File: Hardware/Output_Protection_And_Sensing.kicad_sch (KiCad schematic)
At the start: 8 parts

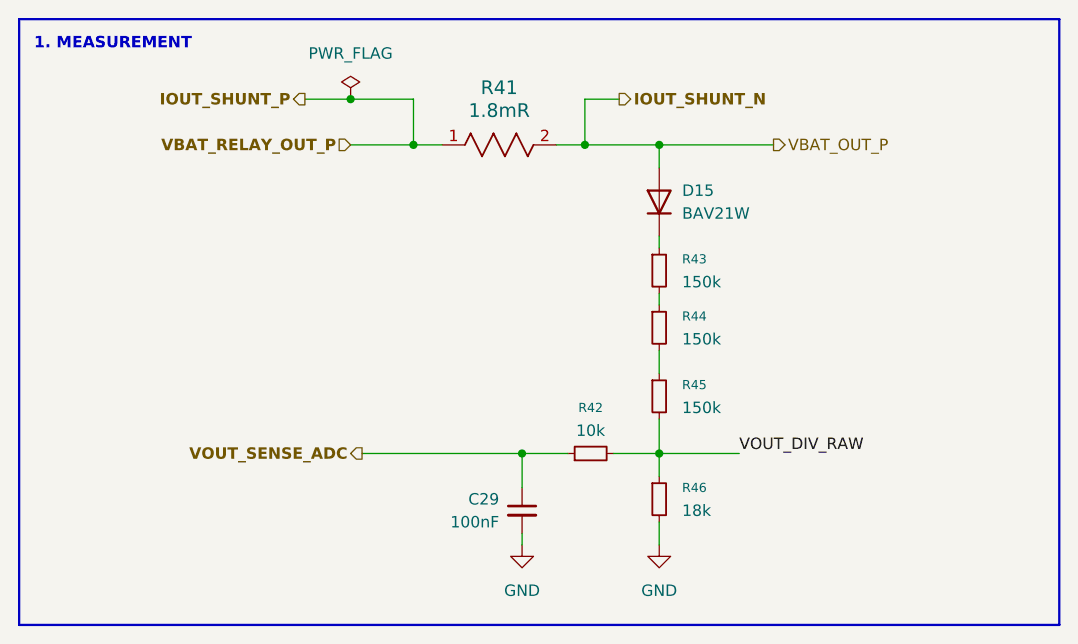
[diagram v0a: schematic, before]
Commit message: feat: update buy link, footprint
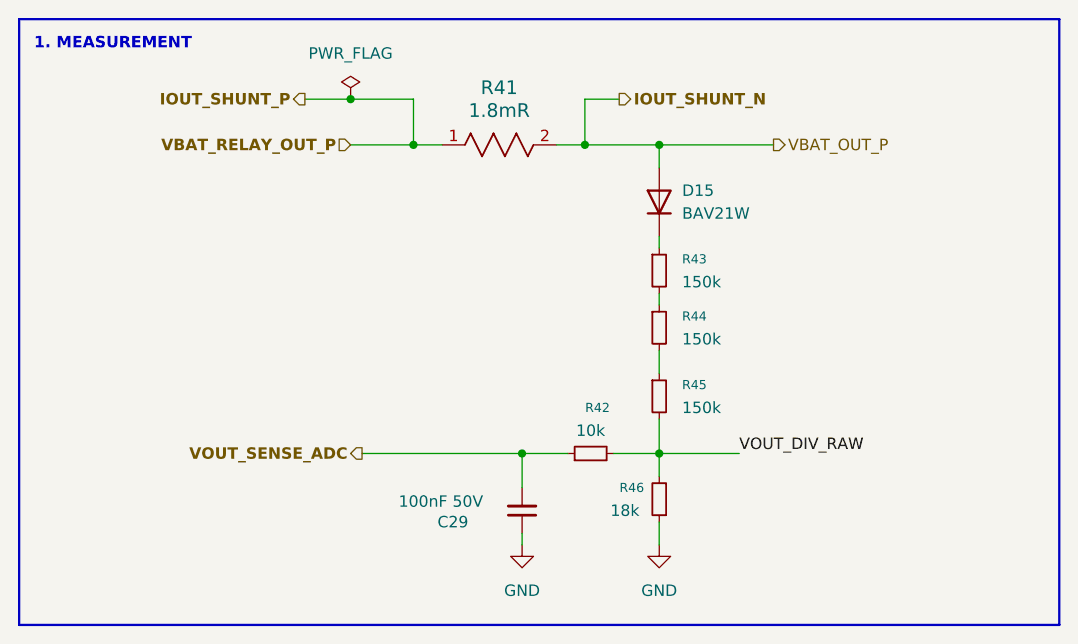
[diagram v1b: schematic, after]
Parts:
- C29: value 100nF -> 100nF 50V; footprint (none) -> Capacitor_SMD:C_0805_2012Metric; Link to Buy (none) -> https://linhkien.cxtvn.com/1976-tu-khong-phan-cuc-0805.html
- D15: footprint Diode_THT:D_DO-35_SOD27_P7.62mm_Horizontal -> Diode_SMD:D_SOD-123; Link to Buy (none) -> https://linhkienthuduc.com/san-pham/bav21w-250v-400ma-sod-1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
- R41: Link to Buy (none) -> https://www.lcsc.com/product-detail/C6490493.html?s_z=n_q_p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
- R42: footprint (none) -> Resistor_SMD:R_0805_2012Metric; Link to Buy (none) -> https://linhkien.cxtvn.com/8792-dien-tro-10k-0805-01-10c.ht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
- R43, R44, R45: footprint (none) -> Resistor_SMD:R_0805_2012Metric; Link to Buy (none) -> https://linhkien.cxtvn.com/6685-dien-tro-0805-1-thong-so-tu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
- R46: footprint (none) -> Resistor_SMD:R_0805_2012Metric; Link to Buy (none) -> https://linhkien.cxtvn.com/4177-dien-tro-0805-1-thong-so-tu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
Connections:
- net GND: now also C29.1, R46.1; no longer C29.2, R46.2
- net VOUT_DIV_RAW: now also R46.2; no longer R46.1
- net VOUT_SENSE_ADC: now also C29.2; no longer C29.1

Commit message: feat: update schematic with new components for communication interfaces and export BOM list
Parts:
- C29: value 100nF 50V -> 100nF
- R41: footprint RES_1L00x_BRN -> CSS2H_2512R_1L00F:RES_1L00x_BRN
- R42: value 10k -> 10kR; Link to Buy https://linhkien.cxtvn.com/8792-dien-tro-10k-0805-01-10c.ht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 -> https://linhkien.cxtvn.com/9909-dien-tro-0805-05-18w-10-chi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
- R43, R44, R45: value 150k -> 150kR
- R46: value 18k -> 18kR
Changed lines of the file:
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@@
 			)
 		)
-		(property "Footprint" "RES_1L00x_BRN"
+		(property "Footprint" "CSS2H_2512R_1L00F:RES_1L00x_BRN"
 			(at 135.89 74.93 0)
 			(hide yes)
@@
 			)
 		)
-		(property "Datasheet" "https://mm.digikey.com/Volume0/opasdata/d220001/medias/docus/5561/BAV19W%20thru%20BAV21W.pdf"
+		(property "Datasheet" "https://mm.digikey.com/Volume0/opasdata/d220001/medias/docus/5335/SOD123AV21WST3.pdf"
 			(at 160.02 81.28 0)
 			(hide yes)
@@
 			)
 		)
-		(property "Value" "10k"
+		(property "Value" "10kR"
 			(at 152.4 106.68 90)
 			(show_name no)
@@
 			)
 		)
-		(property "Link to Buy" "https://linhkien.cxtvn.com/8792-dien-tro-10k-0805-01-10c.html"
+		(property "Link to Buy" "https://linhkien.cxtvn.com/9909-dien-tro-0805-05-18w-10-chiec-cac-gia-tri.html"
 			(at 234.95 -85.09 0)
 			(hide yes)
@@
 			)
 		)
-		(property "Value" "100nF 50V"
+		(property "Value" "100nF"
 			(at 131.064 114.554 0)
 			(show_name no)
@@
 			)
 		)
-		(property "Value" "150k"
+		(property "Value" "150kR"
 			(at 162.56 90.1699 0)
 			(show_name no)
@@
 			)
 		)
-		(property "Value" "150k"
+		(property "Value" "150kR"
 			(at 162.56 104.1399 0)
 			(show_name no)
@@
 			)
 		)
-		(property "Value" "150k"
+		(property "Value" "150kR"
 			(at 162.56 96.5199 0)
 			(show_name no)
@@
 			)
 		)
-		(property "Value" "18k"
+		(property "Value" "18kR"
 			(at 156.21 115.57 0)
 			(show_name no)

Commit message: Refactor code structure for improved readability and maintainability
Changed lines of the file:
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@@
 	(wire
 		(pts
-			(xy 160.02 109.22) (xy 168.91 109.22)
+			(xy 160.02 109.22) (xy 172.72 109.22)
 		)
 		(stroke
@@
 	)
 	(label "VOUT_DIV_RAW"
-		(at 168.91 109.22 0)
+		(at 172.72 109.22 0)
 		(effects
 			(font
